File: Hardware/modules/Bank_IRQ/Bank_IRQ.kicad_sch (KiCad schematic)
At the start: 27 parts, among them J2 Bus_PCI_6502, U1 74HC00, U2 74HC138, U3 6525

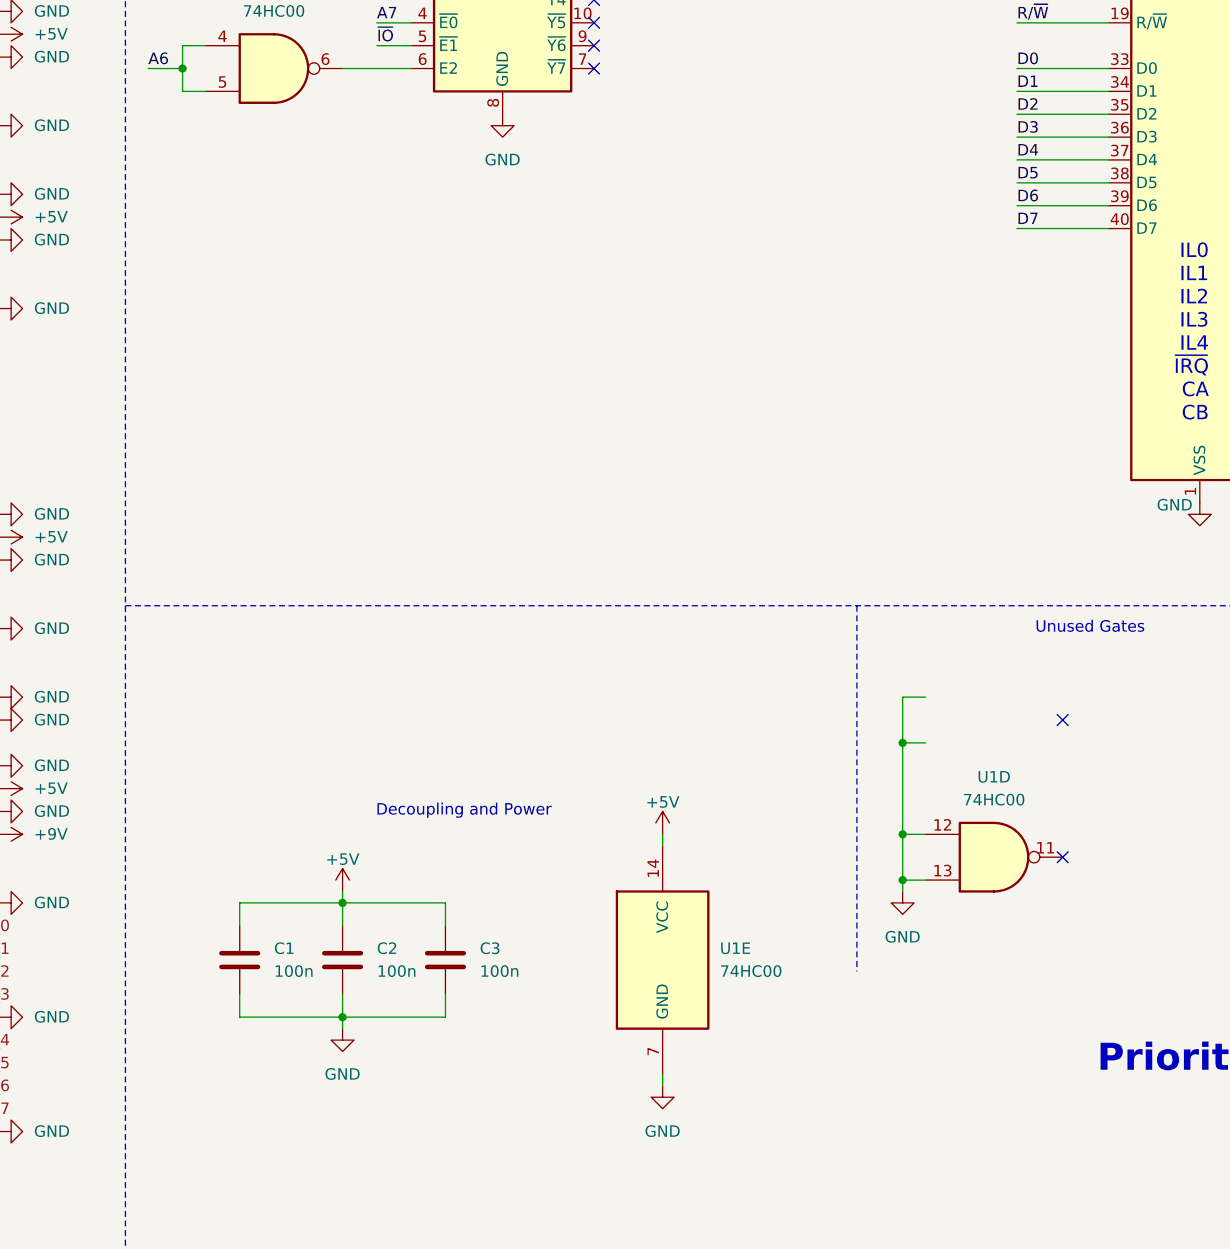
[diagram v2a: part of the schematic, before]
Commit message: Hardware Review Pt. 1 fix Address Decoding for Strobe Generators add bulk capacitance to every board fix wiring of Prototyping Board
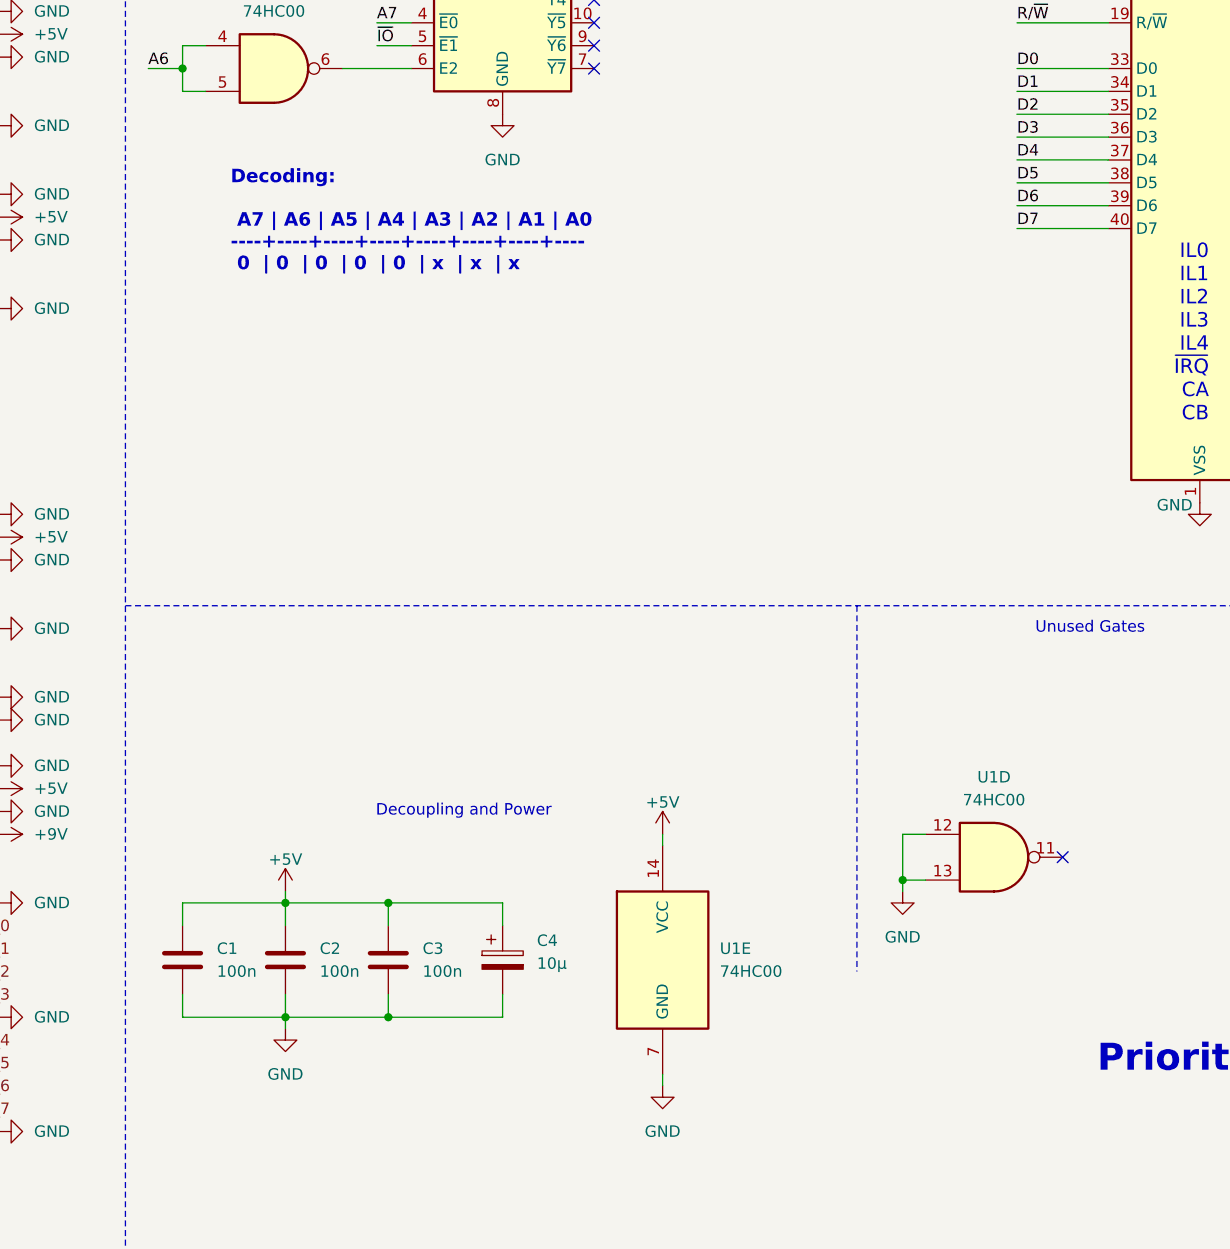
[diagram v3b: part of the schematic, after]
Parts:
- added C4: 10µ, Capacitor_THT:CP_Radial_D5.0mm_P2.50mm, symbol Device:C_Polarized
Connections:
- net +5V: now also C4.1
- net GND: now also C4.2
- no-connect marks 40 -> 39
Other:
- note added: "Decoding: A7 | A6 | A5 | A4 | A3 | A2 | A1 | A0 ----+----+----+----+----+----+----+---- 0 | 0 | 0 | 0 | 0 | x | x | x"
- moved on the sheet: C1, C2, C3
